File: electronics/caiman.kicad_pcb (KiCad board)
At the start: 2 copper layers, 90.9 x 93.9 mm, 134 parts, among them J1 Conn_01x03_Pin, J10 Conn_01x04_Pin, J11 Conn_01x04_Pin, J12 Conn_01x04_Pin, J13 Micro_SD_Card, J14 50 ohm, J15 Conn_01x03_Pin, J2 Conn_01x04_Pin, J3 Conn_01x04_Pin, J4 Conn_01x03_Pin, J5 Conn_01x04_Pin, J6 Conn_01x04_Pin, J7 Conn_01x02_Pin, J8 Conn_01x02_Pin, J9 Conn_01x02_Pin, Q1 Q_PMOS-E_Generic_SSSGD, Q2 AON6262E, U1 AP63205WU, U10 SN74LV1T34DBV, U2 AP63203WU, U3 US1881, U4 LM74700, U5 LPS22HBTR, U6 LIS2MDLTR, U7 STM32F765VITx, U8 LSM6DSO, U9 nRF24L01P, Y1 8MHz, Y2 16MHz

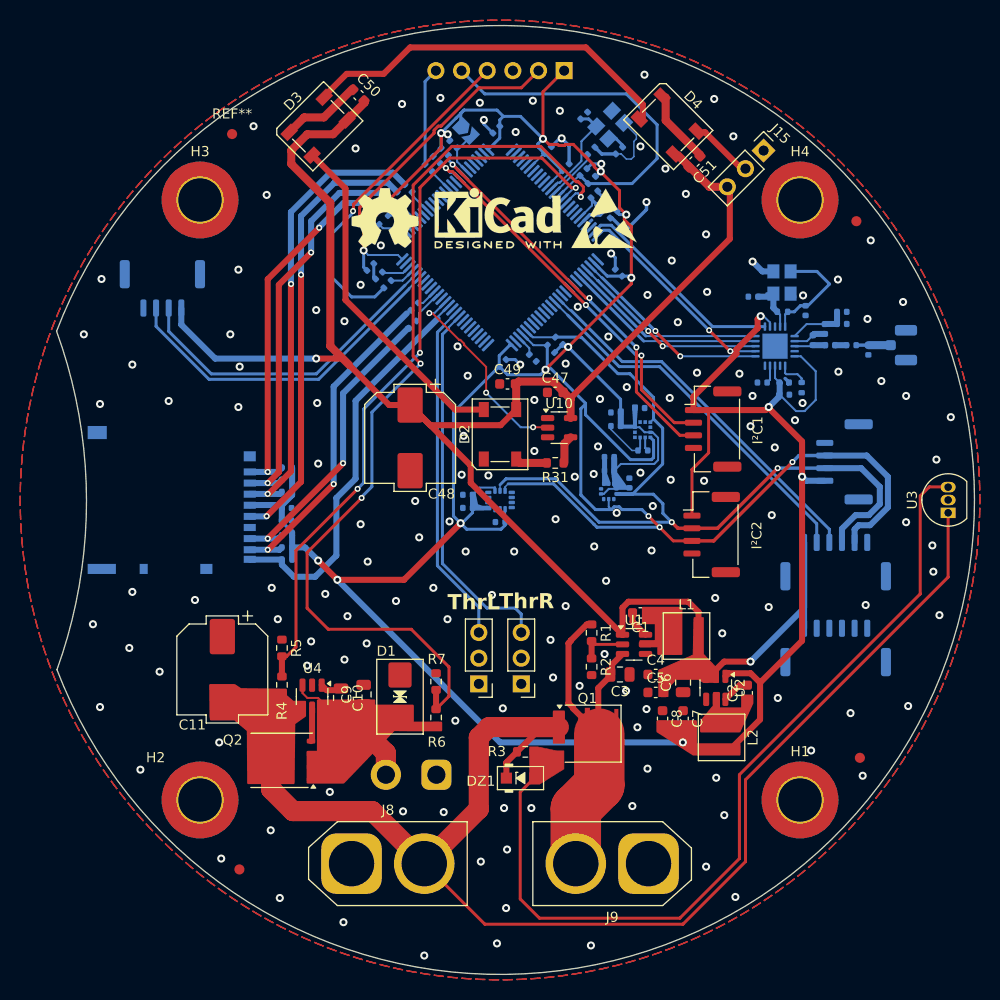
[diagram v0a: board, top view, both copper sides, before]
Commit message: Correct PCB net contacts, add PRe report source, drop AI scratch files
PCB (electronics/caiman.kicad_pcb)
- Eliminate all shorting_items: 5 -> 0. Two GND/+3V3 copper overlaps
  (49 um and 137 um), one +3V3 to /I2C2_SDA overlap and one /CSN to +3V3
  tangency are resolved by moving four vias and deleting one isolated
  stitching via.
- /VBAT was 1e-6 mm from an /I2C1_SCL via; now 0.22 mm.
- Open up the congested SPI and I2C channels by narrowing 110 signal
  tracks to 0.15 mm and shrinking 17 signal vias to 0.5 mm and 6 GND
  vias to 0.6 mm. Annular rings stay at 0.1 mm, twice the 0.075 minimum.
  Signal currents are microamps, so the narrower copper costs nothing.
- Worst clearance improves from 1e-6 mm to 0.1291 mm, above the 0.10 mm
  process capability. Unconnected items stay at 0 throughout.
- Enable island removal on both GND pours, clearing 57 isolated_copper
  warnings. Floating copper serves no purpose and can radiate.
- Thicken 12 silkscreen texts to 0.15 mm and hide 26 reference fields
  that collided on 0402/0603 passives. Assembly uses the CPL file;
  designators stay visible on ICs, crystal and transistor.
- Warnings: 251 -> 133. The remaining 108 lib_footprint_mismatch were
  audited pad by pad against the library: all are metadata, B.Cu
  mirroring, a moved anchor, or the intentional microSD shield
  renumbering. Do not run "Update Footprints from Library" - it would
  undo that renumbering and the hidden references.

Design rules (electronics/caiman.kicad_pro)
- min_hole_to_hole 0.50 -> 0.30 mm. The old value was arbitrary; 0.30
  still leaves 50 percent margin over the 0.20 mm fab capability.

Report (rapport_stage/)
- Add the LaTeX source, figures and evidence for the PRe report.
- Production files are deliberately left out of this commit: the zip
  predates these corrections and must be regenerated from the fixed
  board before any new order.

Cleanup
- Remove AI conversation logs and prompt files.
- Untrack the Streamlit runtime log.
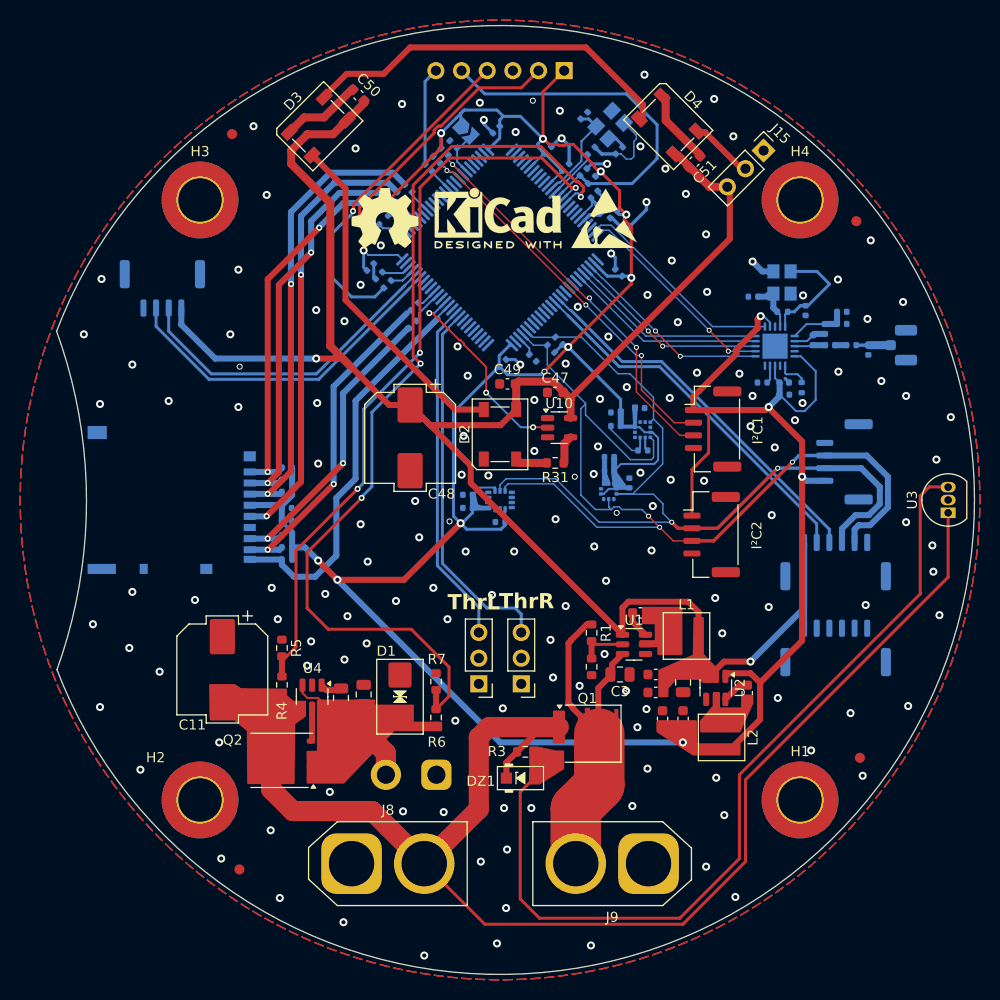
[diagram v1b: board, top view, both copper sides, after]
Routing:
- net GND: track 45.4 -> 46.0 mm, vias 157 -> 156
